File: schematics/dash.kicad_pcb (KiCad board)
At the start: 2 copper layers, 43 x 26 mm, 32 parts, among them J1 BATT_CONN, J2 EXTERNAL_TRIGGER, J3 USB_OTG, J4 Conn_01x08, J5 Conn_01x08, SW1 SW_Push, U1 ESP-12E, U2 ch340g, U3 MCP73833, U4 HT7333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

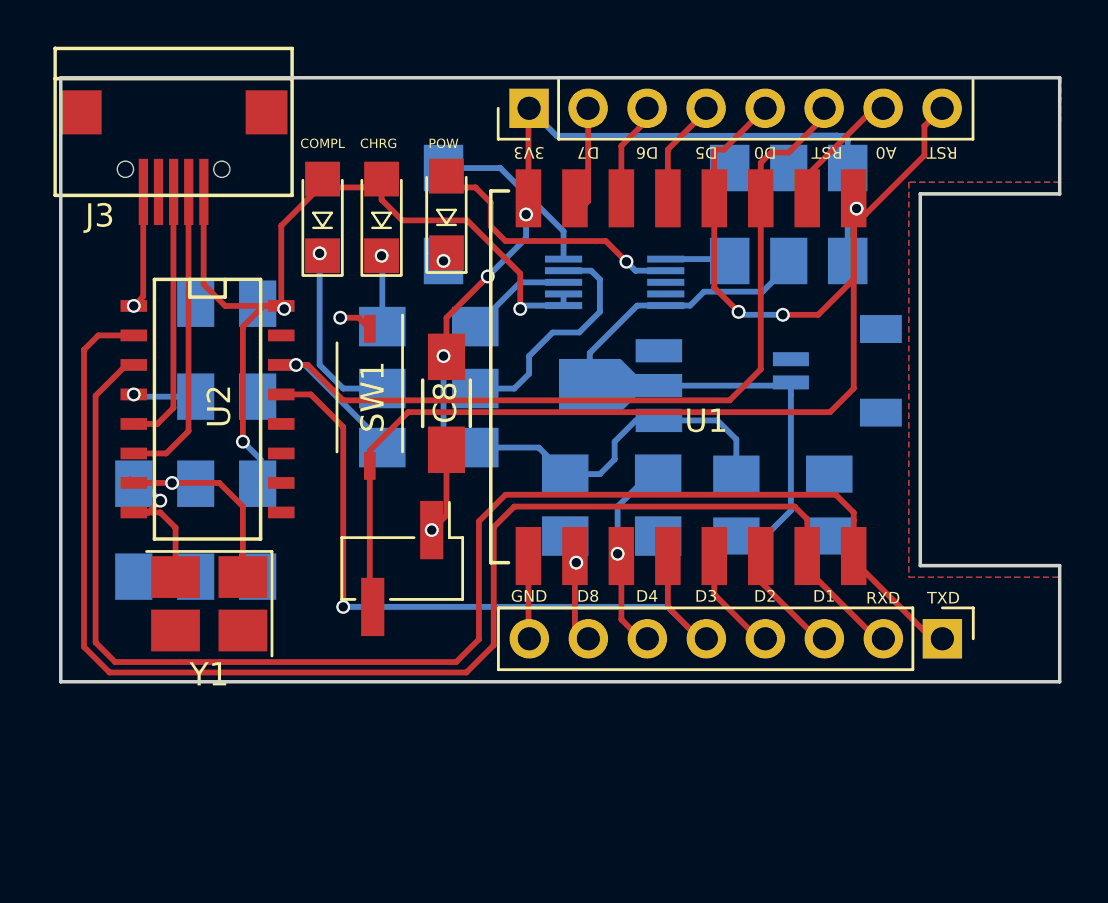
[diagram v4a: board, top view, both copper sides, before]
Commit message: load sharing (USB <-> battery), change to MCP73831
add all lib dependencies locally
restructure dirs
less vias in pads !
change top copper pour to 5V, not 3,3V

type fottprint in readme
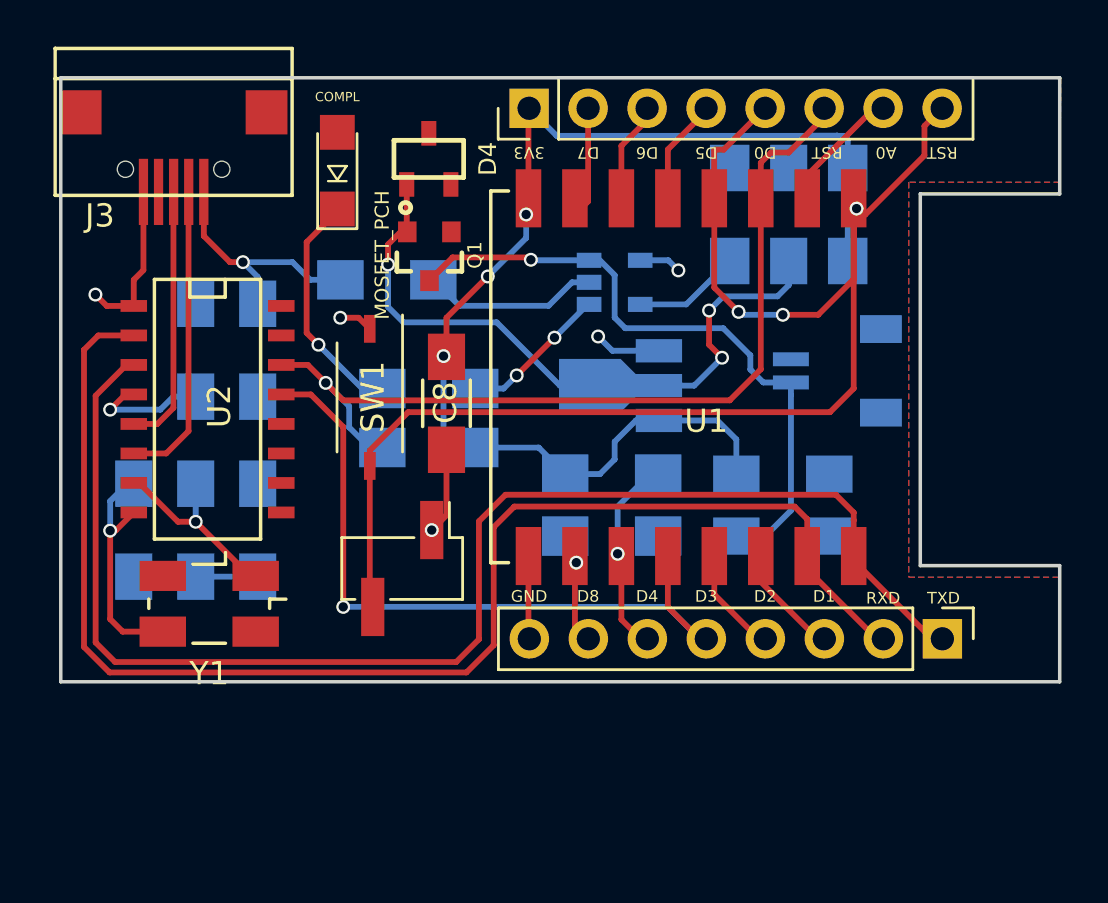
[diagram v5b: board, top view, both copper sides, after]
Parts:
- removed D2: ORANGE, LEDs:LED_1206
- removed D3: RED, LEDs:LED_1206
- removed G***: LOGO, LOGO
- removed R1, R4: 470, Resistors_SMD:R_1206_HandSoldering
- added D4: D_Schottky, sot:SOT23, F.Cu at (148.2, 93.9)
- added Q1: MOSFET_PCH, Silicon-Standard:SOT23-3, F.Cu at (148.2, 98.0)
- added R9: 100k, Resistors_SMD:R_1206_HandSoldering, B.Cu at (146.4, 99.1)
- R3: value 1k -> 10k
- U3: value MCP73833 -> MCP73831; footprint sop:MSOP10 -> sot:SOT23-5
- Y1: footprint Crystals:Crystal_SMD_3225-4pin_3.2x2.5mm_HandSoldering -> Crystals:Crystal_SMD_5032_4Pads
- moved D1 2.11 mm to (144.3, 94.4)
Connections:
- net Net-(C2-Pad1) renamed /XI
- net Net-(C3-Pad1) renamed /XO
- C7 pad 2: Net-(C1-Pad1) -> Net-(C7-Pad2)
- J1 pad 2: Net-(C1-Pad1) -> Net-(C7-Pad2)
- U3 pad 1: +5V -> Net-(R2-Pad1)
- U3 pad 2: +5V -> GND
- U3 pad 3: Net-(R1-Pad2) -> Net-(C7-Pad2)
- U3 pad 4: Net-(R2-Pad1) -> +5V
- U3 pad 5: GND -> Net-(R3-Pad2)
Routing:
- net Net-(C7-Pad2): track 0.00 -> 28.0 mm, vias 0 -> 1
- net +5V: track 39.3 -> 12.5 mm, vias 3 -> 2
- net Net-(D3-Pad2): track 11.6 -> 0.00 mm, vias 1 -> 0
- net GND: track 24.5 -> 33.7 mm, vias 3 -> 4
- net Net-(R1-Pad2): track 4.59 -> 0.00 mm
- net Net-(R2-Pad1): track 10.3 -> 6.40 mm, vias 0 -> 2
- net /XO: track 7.21 -> 10.5 mm
- net Net-(D2-Pad1): track 3.06 -> 0.00 mm, vias 1 -> 0
- net Net-(C6-Pad1): track 2.71 -> 5.20 mm
- net Net-(R3-Pad2): track 2.79 -> 4.74 mm
- net Net-(D3-Pad1): track 1.93 -> 0.00 mm, vias 1 -> 0
- net Net-(D1-Pad1): track 8.41 -> 10.1 mm
- net /CH_PD: track 40.6 -> 39.0 mm
- net Net-(C1-Pad1): track 28.8 -> 29.5 mm, vias 0 -> 3
- added copper zone on F.Cu, net +5V
- removed copper zone on F.Cu, net +3V3
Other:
- board text removed: "CHRG"
- board text removed: "POW"

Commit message: finish routing
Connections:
- J3 pad 6: Net-(J3-Pad6) -> GND
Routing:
- net GND: track 33.7 -> 58.5 mm, vias 4 -> 6
- net +5V: track 12.5 -> 22.2 mm, vias 2 -> 3
- net /GPIO15: track 8.44 -> 6.97 mm

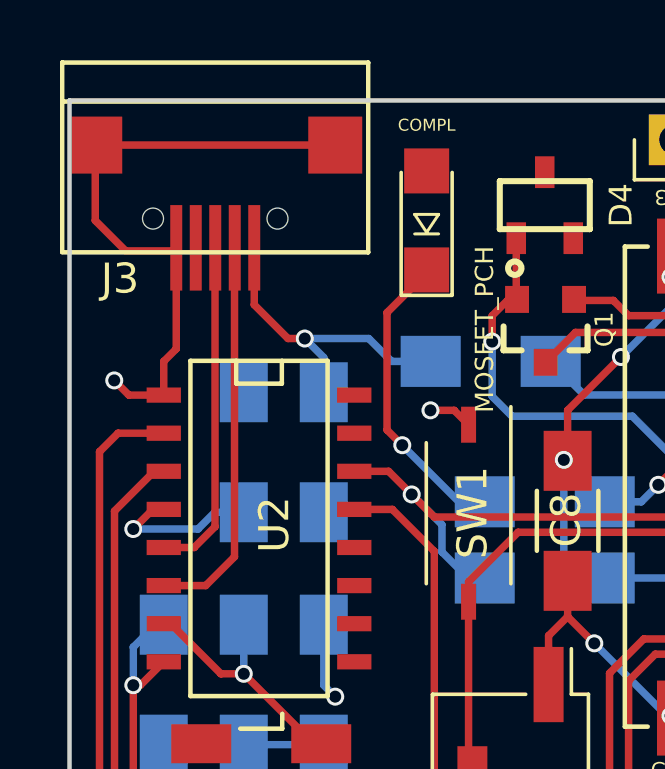
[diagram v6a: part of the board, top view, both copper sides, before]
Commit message: swap USB connector for a THT one
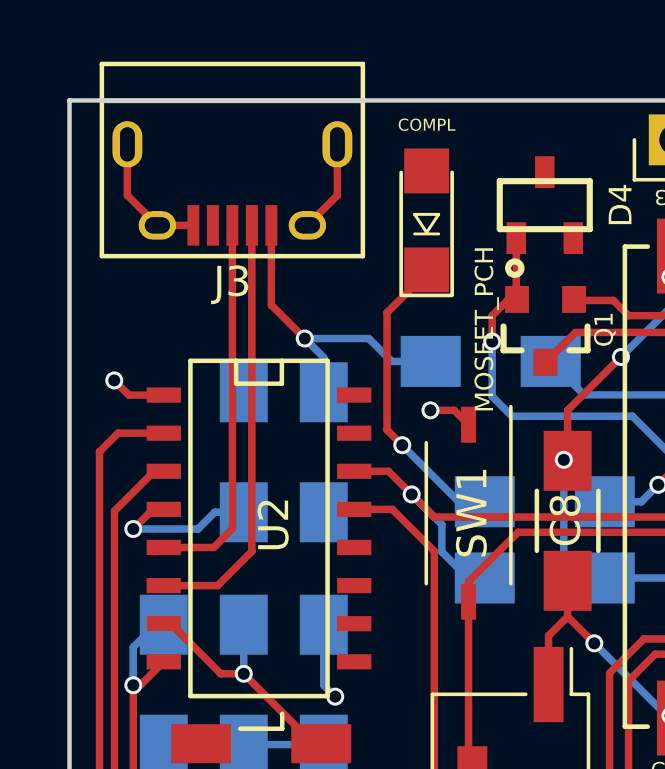
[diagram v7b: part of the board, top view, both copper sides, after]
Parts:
- J3: footprint kicad-rleh/USB_Mikro_SMD_China.pretty:USB_Micro_SMD_China -> Connect:USB_Micro-B
- moved J3 1.66 mm to (137.8, 93.0), turned to 180 degrees
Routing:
- net GND: track 58.5 -> 47.2 mm
- net /D+: track 12.1 -> 12.7 mm

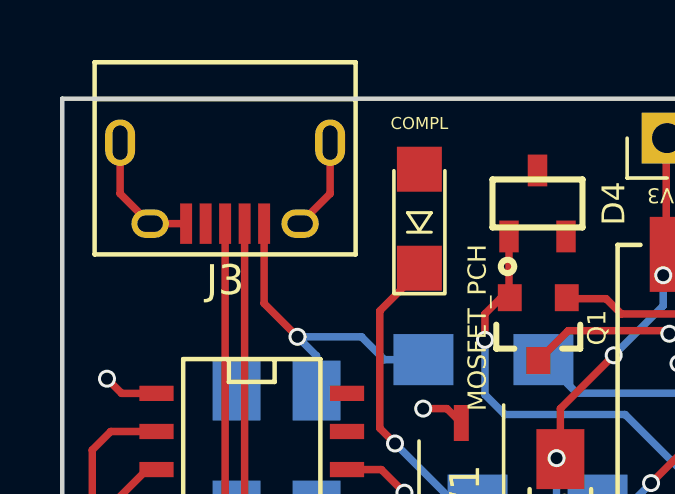
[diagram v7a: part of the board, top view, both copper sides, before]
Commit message: change USB connector to custom
add URLAB logo
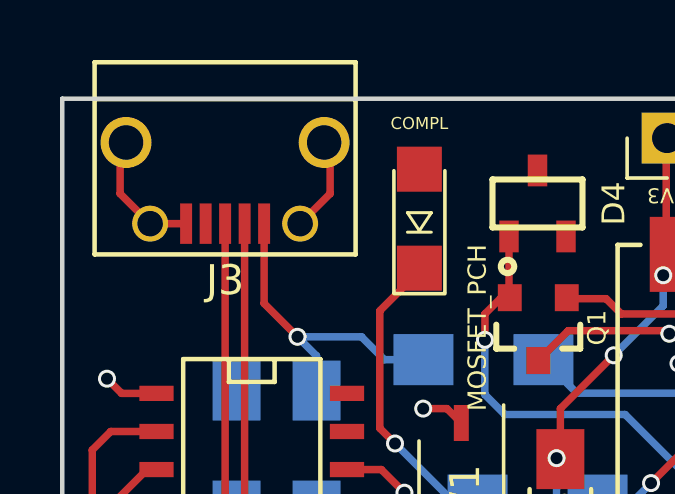
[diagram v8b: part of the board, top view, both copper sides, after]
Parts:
- added URLAB-LOGO1: logo, custom-cheddar:urlab, B.Cu at (147.1, 110.6)
